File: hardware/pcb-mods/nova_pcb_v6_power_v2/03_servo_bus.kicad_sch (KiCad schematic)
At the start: 11 parts, among them J3 XT30_Inj, J4 XT30_Inj, J5 XT30_Inj, J6 XT30_Inj, J7 XT30_Inj, J8 ServoBus_TTL

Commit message: pcb(v6-power-v2): backfill MPN + Manufacturer fields — 100% BOM coverage
All 50 BOM components now carry MPNs from the verified order list:
Yageo RC0603 resistor set (R14 470k = Vishay CRCW0603 DigiKey sub),
Nichicon UPW1E bulk caps, Bourns SRR1260-220M, Infineon IRLB3034PBF,
onsemi BSS138 x3, TI LM393DR, Pololu buck modules (off-board),
GODIY INA226 20A R002 modules with I2C addresses in Manufacturer field,
AMASS XT60H/XT30U, JST B3B-XH-A, Adam Tech BHR-12-VUA, Sullins headers.
ERC: 0 errors (1 expected V7V5_ARM warning). kicad-happy bom_lock: pass.

Co-Authored-By: Claude Fable 5 <noreply@anthropic.com>
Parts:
- C1, C2, C3, C4, C5: MPN (none) -> UPW1E102MPD6; Manufacturer (none) -> Nichicon
- J3, J4, J5, J6, J7: MPN (none) -> XT30U-M; Manufacturer (none) -> AMASS
- J8: MPN (none) -> B3B-XH-A; Manufacturer (none) -> JST
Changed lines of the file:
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@@
+			)
+		)
+		(property "Manufacturer" "AMASS" (at 0 0 0)
+			(effects
+				(font
+					(size 1.27 1.27)
+				)
+				(hide yes)
+			)
+		)
+		(property "MPN" "XT30U-M" (at 0 0 0)
+			(effects
+				(font
+					(size 1.27 1.27)
+				)
+				(hide yes)
 			)
 		)
@@
 			)
 		)
+		(property "Manufacturer" "Nichicon" (at 0 0 0)
+			(effects
+				(font
+					(size 1.27 1.27)
+				)
+				(hide yes)
+			)
+		)
+		(property "MPN" "UPW1E102MPD6" (at 0 0 0)
+			(effects
+				(font
+					(size 1.27 1.27)
+				)
+				(hide yes)
+			)
+		)
 		(pin "1"
 		)
@@
 			)
 		)
+		(property "Manufacturer" "JST" (at 0 0 0)
+			(effects
+				(font
+					(size 1.27 1.27)
+				)
+				(hide yes)
+			)
+		)
+		(property "MPN" "B3B-XH-A" (at 0 0 0)
+			(effects
+				(font
+					(size 1.27 1.27)
+				)
+				(hide yes)
+			)
+		)
 		(pin "1"
 		)
@@
 			)
 		)
+		(property "Manufacturer" "Nichicon" (at 0 0 0)
+			(effects
+				(font
+					(size 1.27 1.27)
+				)
+				(hide yes)
+			)
+		)
+		(property "MPN" "UPW1E102MPD6" (at 0 0 0)
+			(effects
+				(font
+					(size 1.27 1.27)
+				)
+				(hide yes)
+			)
+		)
 		(pin "1"
 		)
@@
 			)
 		)
+		(property "Manufacturer" "AMASS" (at 0 0 0)
+			(effects
+				(font
+					(size 1.27 1.27)
+				)
+				(hide yes)
+			)
+		)
+		(property "MPN" "XT30U-M" (at 0 0 0)
+			(effects
+				(font
+					(size 1.27 1.27)
+				)
+				(hide yes)
+			)
+		)
 		(pin "1"
 		)
@@
 			)
 		)
+		(property "Manufacturer" "AMASS" (at 0 0 0)
+			(effects
+				(font
+					(size 1.27 1.27)
+				)
+				(hide yes)
+			)
+		)
+		(property "MPN" "XT30U-M" (at 0 0 0)
+			(effects
+				(font
+					(size 1.27 1.27)
+				)
+				(hide yes)
+			)
+		)
 		(pin "1"
 		)
@@
 			)
 		)
+		(property "Manufacturer" "Nichicon" (at 0 0 0)
+			(effects
+				(font
+					(size 1.27 1.27)
+				)
+				(hide yes)
+			)
+		)
+		(property "MPN" "UPW1E102MPD6" (at 0 0 0)
+			(effects
+				(font
+					(size 1.27 1.27)
+				)
+				(hide yes)
+			)
+		)
 		(pin "1"
 		)
@@
 			)
 		)
+		(property "Manufacturer" "AMASS" (at 0 0 0)
+			(effects
+				(font
+					(size 1.27 1.27)
+				)
+				(hide yes)
+			)
+		)
+		(property "MPN" "XT30U-M" (at 0 0 0)
+			(effects
+				(font
+					(size 1.27 1.27)
+				)
+				(hide yes)
+			)
+		)
 		(pin "1"
 		)
@@
 			)
 		)
+		(property "Manufacturer" "Nichicon" (at 0 0 0)
+			(effects
+				(font
+					(size 1.27 1.27)
+				)
+				(hide yes)
+			)
+		)
+		(property "MPN" "UPW1E102MPD6" (at 0 0 0)
+			(effects
+				(font
+					(size 1.27 1.27)
+				)
+				(hide yes)
+			)
+		)
 		(pin "1"
 		)
@@
 			)
 		)
+		(property "Manufacturer" "Nichicon" (at 0 0 0)
+			(effects
+				(font
+					(size 1.27 1.27)
+				)
+				(hide yes)
+			)
+		)
+		(property "MPN" "UPW1E102MPD6" (at 0 0 0)
+			(effects
+				(font
+					(size 1.27 1.27)
+				)
+				(hide yes)
+			)
+		)
 		(pin "1"
 		)
@@
 			)
 		)
+		(property "Manufacturer" "AMASS" (at 0 0 0)
+			(effects
+				(font
+					(size 1.27 1.27)
+				)
+				(hide yes)
+			)
+		)
+		(property "MPN" "XT30U-M" (at 0 0 0)
+			(effects
+				(font
+					(size 1.27 1.27)
+				)
+				(hide yes)
+			)
+		)

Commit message: pcb(v6-power-v2): correct C1-C5 to FymuSing (as purchased) + DigiKey PNs from order CSV
Verified against Complete_Digikey_Order_NOVA.csv (16 lines, all match):
R14 470k confirmed Vishay CRCW0603470KFKEA (541-470KHCT-ND).
C1-C5 corrected Nichicon->FymuSing 1000uF/25V (Amazon purchase, 10x17mm).
Remaining 23 parts without DigiKey PN are Amazon/Pololu/AMASS sourced.

Co-Authored-By: Claude Fable 5 <noreply@anthropic.com>
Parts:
- C1, C2, C3, C4, C5: MPN UPW1E102MPD6 -> FymuSing-1000uF-25V; Manufacturer Nichicon -> FymuSing (Amazon, 10x17mm, 4mm pitch)
- J8: DigiKey (none) -> 455-2248-ND
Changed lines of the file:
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@@
 			)
 		)
-		(property "Manufacturer" "Nichicon" (at 0 0 0)
-			(effects
-				(font
-					(size 1.27 1.27)
-				)
-				(hide yes)
-			)
-		)
-		(property "MPN" "UPW1E102MPD6" (at 0 0 0)
+		(property "Manufacturer" "FymuSing (Amazon, 10x17mm, 4mm pitch)" (at 0 0 0)
+			(effects
+				(font
+					(size 1.27 1.27)
+				)
+				(hide yes)
+			)
+		)
+		(property "MPN" "FymuSing-1000uF-25V" (at 0 0 0)
 			(effects
 				(font
@@
 			)
 		)
+		(property "DigiKey" "455-2248-ND" (at 0 0 0)
+			(effects
+				(font
+					(size 1.27 1.27)
+				)
+				(hide yes)
+			)
+		)
 		(pin "1"
 		)
@@
 			)
 		)
-		(property "Manufacturer" "Nichicon" (at 0 0 0)
-			(effects
-				(font
-					(size 1.27 1.27)
-				)
-				(hide yes)
-			)
-		)
-		(property "MPN" "UPW1E102MPD6" (at 0 0 0)
+		(property "Manufacturer" "FymuSing (Amazon, 10x17mm, 4mm pitch)" (at 0 0 0)
+			(effects
+				(font
+					(size 1.27 1.27)
+				)
+				(hide yes)
+			)
+		)
+		(property "MPN" "FymuSing-1000uF-25V" (at 0 0 0)
 			(effects
 				(font
@@
 			)
 		)
-		(property "Manufacturer" "Nichicon" (at 0 0 0)
-			(effects
-				(font
-					(size 1.27 1.27)
-				)
-				(hide yes)
-			)
-		)
-		(property "MPN" "UPW1E102MPD6" (at 0 0 0)
+		(property "Manufacturer" "FymuSing (Amazon, 10x17mm, 4mm pitch)" (at 0 0 0)
+			(effects
+				(font
+					(size 1.27 1.27)
+				)
+				(hide yes)
+			)
+		)
+		(property "MPN" "FymuSing-1000uF-25V" (at 0 0 0)
 			(effects
 				(font
@@
 			)
 		)
-		(property "Manufacturer" "Nichicon" (at 0 0 0)
-			(effects
-				(font
-					(size 1.27 1.27)
-				)
-				(hide yes)
-			)
-		)
-		(property "MPN" "UPW1E102MPD6" (at 0 0 0)
+		(property "Manufacturer" "FymuSing (Amazon, 10x17mm, 4mm pitch)" (at 0 0 0)
+			(effects
+				(font
+					(size 1.27 1.27)
+				)
+				(hide yes)
+			)
+		)
+		(property "MPN" "FymuSing-1000uF-25V" (at 0 0 0)
 			(effects
 				(font
@@
 			)
 		)
-		(property "Manufacturer" "Nichicon" (at 0 0 0)
-			(effects
-				(font
-					(size 1.27 1.27)
-				)
-				(hide yes)
-			)
-		)
-		(property "MPN" "UPW1E102MPD6" (at 0 0 0)
-			(effects
-				(font
+		(property "Manufacturer" "FymuSing (Amazon, 10x17mm, 4mm pitch)" (at 0 0 0)
+			(effects
+				(font
+					(size 1.27 1.27)
+				)
+				(hide yes)
+			)
+		)
+		(property "MPN" "FymuSing-1000uF-25V" (at 0 0 0)
+			(effects
+				(font

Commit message: pcb(v6-power-v2): AssemblyOrder fields + assembly-sequenced iBOM
15-step hand-solder sequence (flat->tall, SMD bottom cluster -> THT top):
0603s -> SOT-23 -> SOIC -> L1 -> INA headers -> headers/JST/IDC ->
screw blocks -> XT30 -> XT60 -> Q1 (Step 10a test first) -> 470uF -> 1000uF.
bom/ibom_assembly.html groups by AssemblyOrder via netlist extra-data.

Co-Authored-By: Claude Fable 5 <noreply@anthropic.com>
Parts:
- C1, C2, C3, C4, C5: AssemblyOrder (none) -> 15 THT 1000uF tallest last
- J3, J4, J5, J6, J7: AssemblyOrder (none) -> 11 THT XT30
- J8: AssemblyOrder (none) -> 08 THT JST
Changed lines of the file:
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@@
+			)
+		)
+		(property "AssemblyOrder" "11 THT XT30" (at 0 0 0)
+			(effects
+				(font
+					(size 1.27 1.27)
+				)
+				(hide yes)
 			)
 		)
@@
 			)
 		)
+		(property "AssemblyOrder" "15 THT 1000uF tallest last" (at 0 0 0)
+			(effects
+				(font
+					(size 1.27 1.27)
+				)
+				(hide yes)
+			)
+		)
 		(pin "1"
 		)
@@
 			)
 		)
+		(property "AssemblyOrder" "08 THT JST" (at 0 0 0)
+			(effects
+				(font
+					(size 1.27 1.27)
+				)
+				(hide yes)
+			)
+		)
 		(pin "1"
 		)
@@
 			)
 		)
+		(property "AssemblyOrder" "15 THT 1000uF tallest last" (at 0 0 0)
+			(effects
+				(font
+					(size 1.27 1.27)
+				)
+				(hide yes)
+			)
+		)
 		(pin "1"
 		)
@@
 			)
 		)
+		(property "AssemblyOrder" "11 THT XT30" (at 0 0 0)
+			(effects
+				(font
+					(size 1.27 1.27)
+				)
+				(hide yes)
+			)
+		)
 		(pin "1"
 		)
@@
 			)
 		)
+		(property "AssemblyOrder" "11 THT XT30" (at 0 0 0)
+			(effects
+				(font
+					(size 1.27 1.27)
+				)
+				(hide yes)
+			)
+		)
 		(pin "1"
 		)
@@
 			)
 		)
+		(property "AssemblyOrder" "15 THT 1000uF tallest last" (at 0 0 0)
+			(effects
+				(font
+					(size 1.27 1.27)
+				)
+				(hide yes)
+			)
+		)
 		(pin "1"
 		)
@@
 			)
 		)
+		(property "AssemblyOrder" "11 THT XT30" (at 0 0 0)
+			(effects
+				(font
+					(size 1.27 1.27)
+				)
+				(hide yes)
+			)
+		)
 		(pin "1"
 		)
@@
 			)
 		)
+		(property "AssemblyOrder" "15 THT 1000uF tallest last" (at 0 0 0)
+			(effects
+				(font
+					(size 1.27 1.27)
+				)
+				(hide yes)
+			)
+		)
 		(pin "1"
 		)
@@
 			)
 		)
+		(property "AssemblyOrder" "15 THT 1000uF tallest last" (at 0 0 0)
+			(effects
+				(font
+					(size 1.27 1.27)
+				)
+				(hide yes)
+			)
+		)
 		(pin "1"
 		)
@@
 			(effects
 				(font
+					(size 1.27 1.27)
+				)
+				(hide yes)
+			)
+		)
+		(property "AssemblyOrder" "11 THT XT30" (at 0 0 0)
+			(effects
+				(font

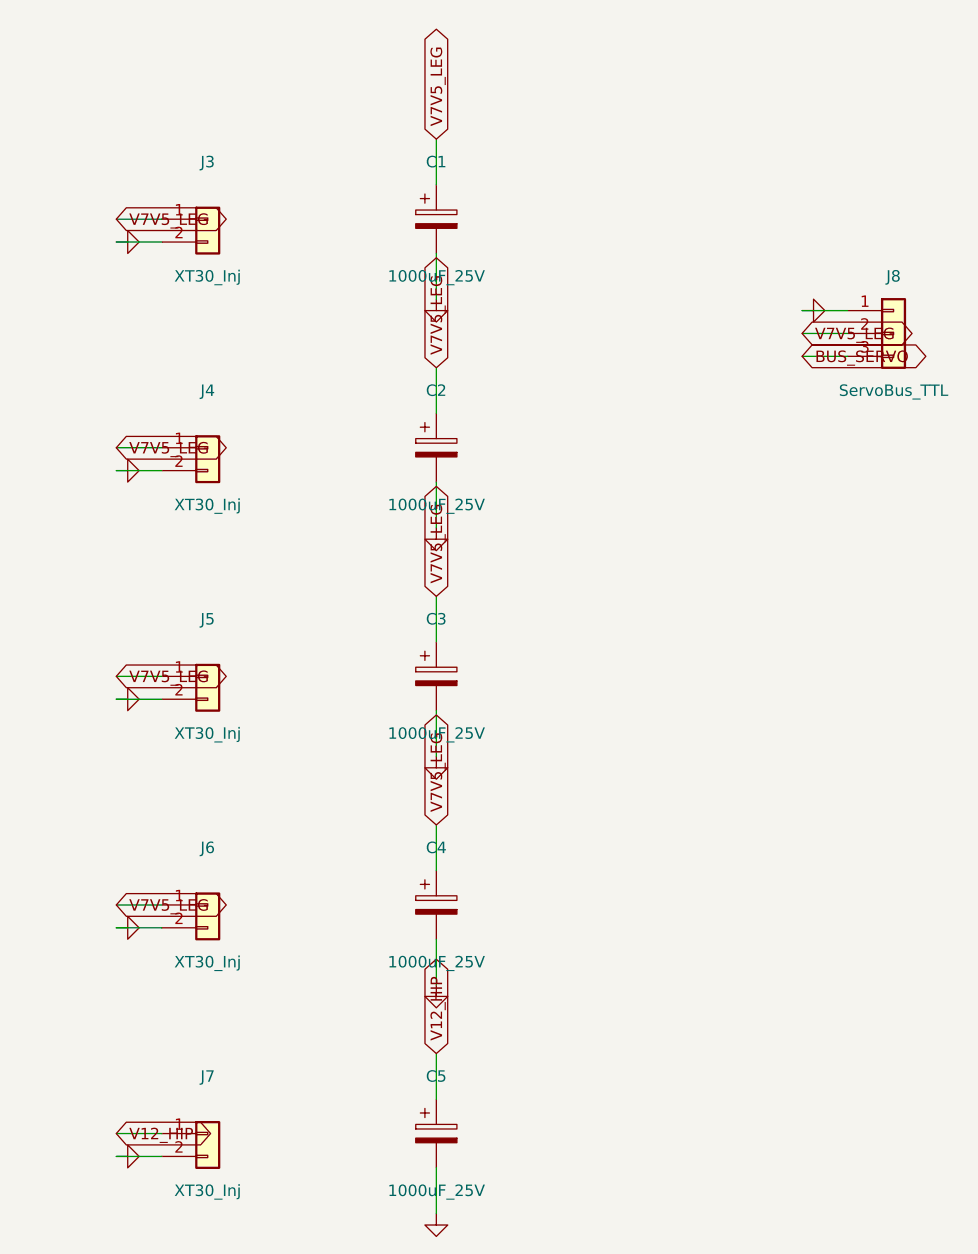
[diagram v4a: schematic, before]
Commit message: power board: fix reversed XT connector polarity (all 9 AMASS XT)
AMASS XT footprints number pad1=chamfer/NEGATIVE, pad2=flat/POSITIVE.
Board had +V wired to pad1 -> every keyed power connector reverse-wired:
J1 (XT60 battery in), J3-J7 (rail injection), J12-J14 (Jetson/L2/arm out).
Mating a normally-built cable would feed +V to the - terminal and fry the
connected load (Jetson, servos, arm). Confirmed against footprint flat/chamfer
geometry + physical connector (flat=+).

Fix: swapped pin1/pin2 net assignment on all 9 connectors in schematic,
re-routed PCB, regenerated 14-file gerber set. Pololu bucks use a custom
non-keyed terminal (pad1=rect=+V) and were correctly left unchanged.

Verify: ERC 0, DRC 0 hard / 0 unconnected, fab_gate GO, J20 match intact.

Co-Authored-By: Claude Opus 4.8 <noreply@anthropic.com>
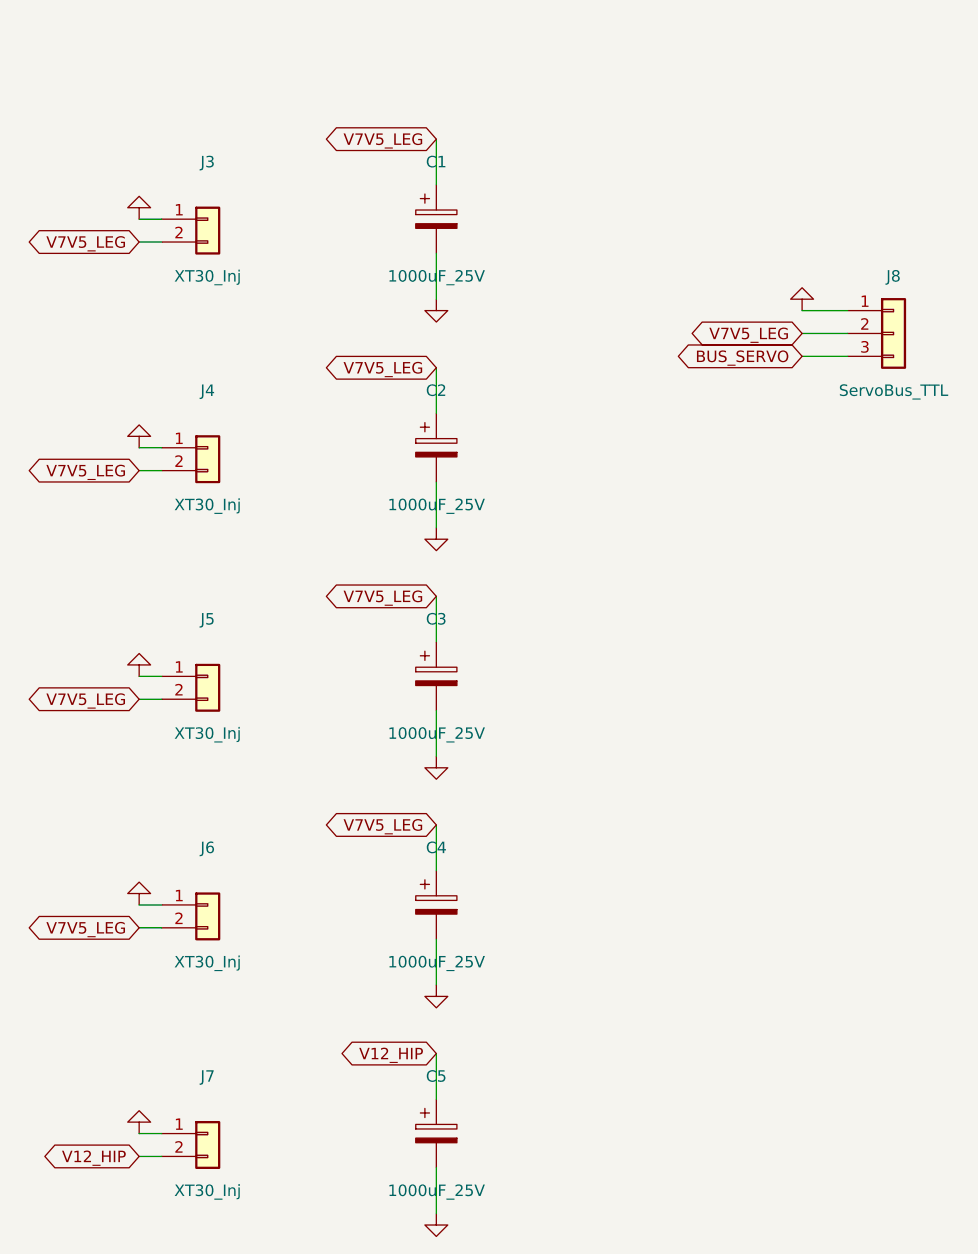
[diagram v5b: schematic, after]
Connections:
- net GND: now also J3.1 (Pin_1), J4.1 (Pin_1), J5.1 (Pin_1), J6.1 (Pin_1), J7.1 (Pin_1); no longer J3.2 (Pin_2), J4.2 (Pin_2), J5.2 (Pin_2), J6.2 (Pin_2), J7.2 (Pin_2)
- net V12_HIP: now also J7.2 (Pin_2); no longer J7.1 (Pin_1)
- net V7V5_LEG: now also J3.2 (Pin_2), J4.2 (Pin_2), J5.2 (Pin_2), J6.2 (Pin_2); no longer J3.1 (Pin_1), J4.1 (Pin_1), J5.1 (Pin_1), J6.1 (Pin_1)
